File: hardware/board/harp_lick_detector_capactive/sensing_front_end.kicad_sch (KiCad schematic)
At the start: 33 parts

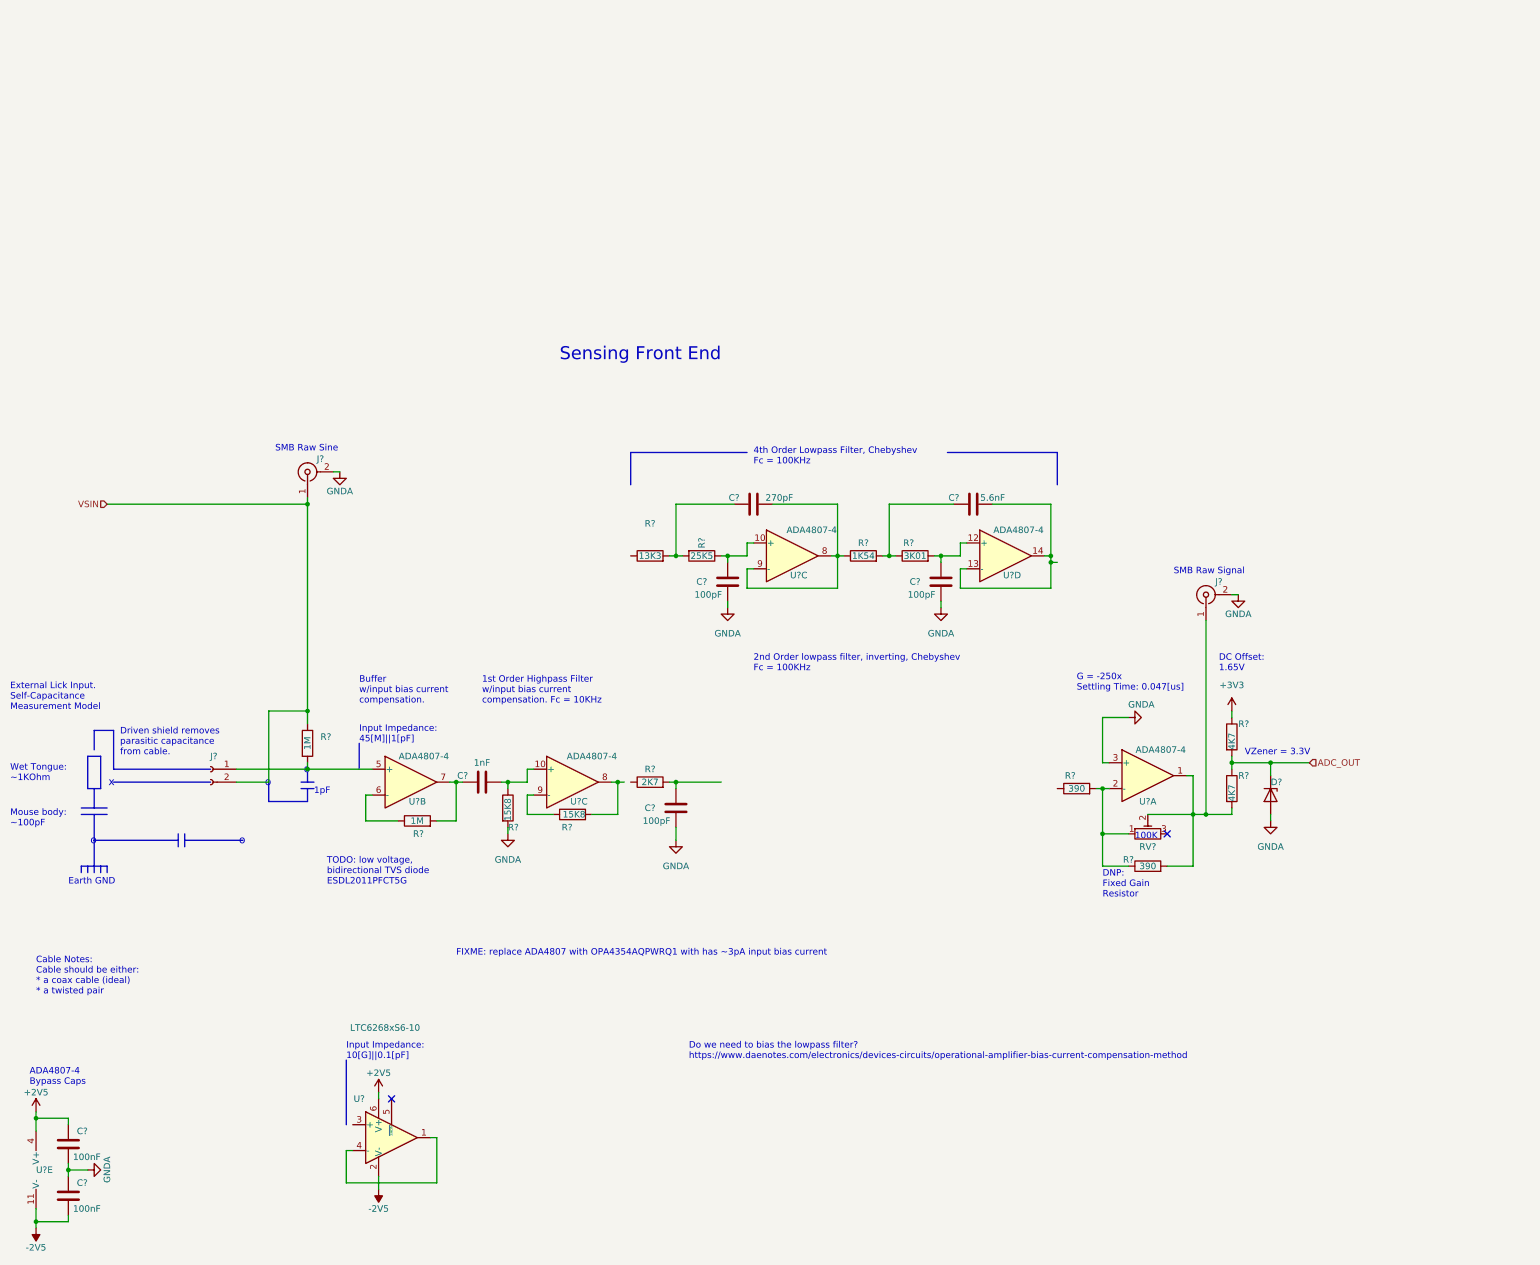
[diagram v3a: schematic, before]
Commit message: document stray capacitances
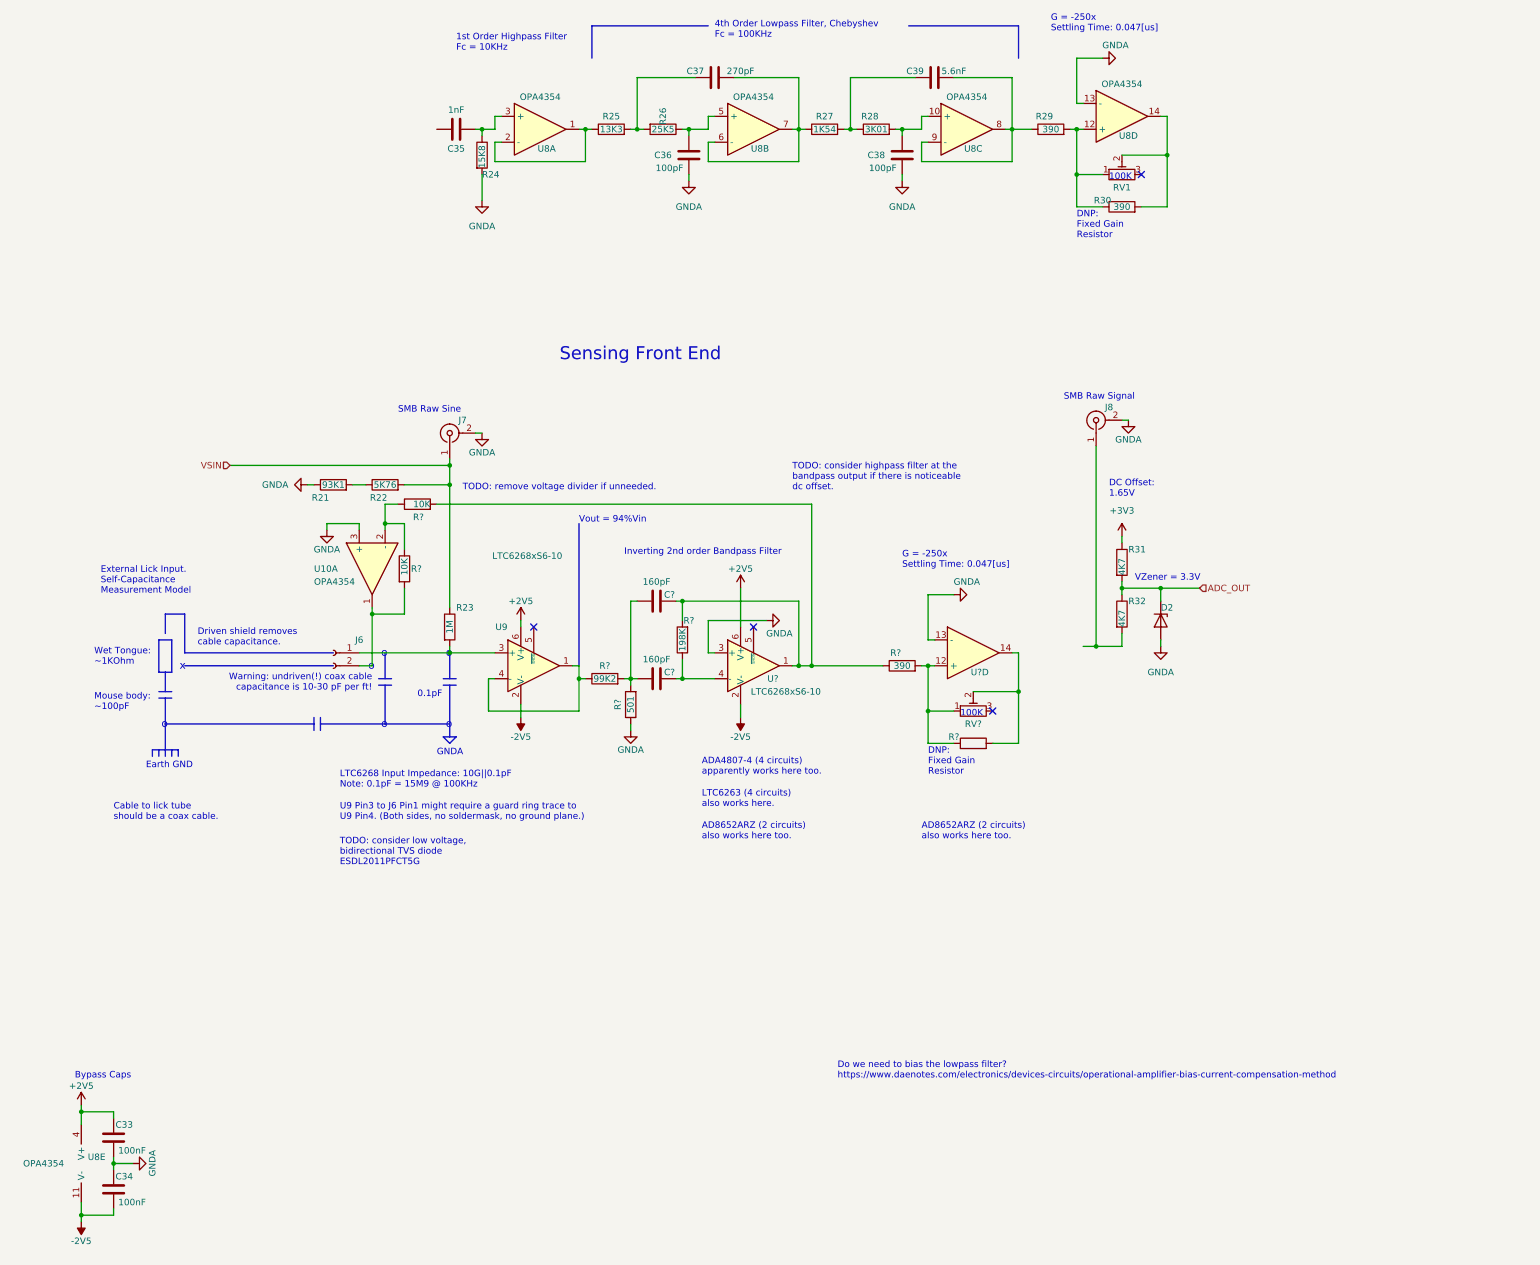
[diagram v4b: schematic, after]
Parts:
- removed C?: 100pF, Capacitor_SMD:C_0603_1608Metric_Pad1.08x0.95mm_HandSolder, symbol Device:C
- removed R?: 2K7, symbol Device:R
- removed R?: 15K8, symbol Device:R
- removed R?: 1M, Resistor_SMD:R_0603_1608Metric_Pad0.98x0.95mm_HandSolder, symbol Device:R
- removed U? (x6): ADA4807-4, Package_SO:TSSOP-14_4.4x5mm_P0.65mm, symbol Amplifier_Operational:ADA4807-4
- added C? (x2): 160pF, Capacitor_SMD:C_0402_1005Metric_Pad0.74x0.62mm_HandSolder, symbol Device:C
- added R21: 93K1, symbol Device:R
- added R22: 5K76, symbol Device:R
- added R?: ~, symbol Device:R
- added R?: 99K2, symbol Device:R
- added R?: 198K, symbol Device:R
- added R?: 501, symbol Device:R
- added R?: 390, symbol Device:R
- added R? (x2): 10K, Resistor_SMD:R_0402_1005Metric_Pad0.72x0.64mm_HandSolder, symbol Device:R
- added RV?: ~, symbol Device:R_Potentiometer_Trim
- added U10, U8: OPA4354, symbol machine_agency_components:OPA4354
- added U?: ~, symbol machine_agency_components:OPA4354
- added U?: LTC6268xS6-10, symbol Amplifier_Operational:LTC6268xS6-10
- gave numbers to parts that had none: 23
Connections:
- net +2V5: now also U8.4 (V+), U?.6 (V+)
- net -2V5: now also U8.11 (V-), U?.2 (V-)
- net GNDA: now also R21.1, R?.1, U10.3 (+), U8.13 (-), U?.13 (-), U?.3 (+)
- net VSIN: now also R22.2; no longer J6.2 (Pin_2)
- net at C38.2, R28.2: now also U8.10 (+)
- net at C39.2: now also R29.1, U8.8, U8.9 (-)
- net at U9.1, U9.4 (-): now also R?.1
- net at U9.3 (+): now also J6.1 (Pin_1), R23.2
- net at R25.1: now also U8.1, U8.2 (-)
- net at C36.2, R26.1: now also U8.5 (+)
- net at C35.2, R24.1: now also U8.3 (+)
- net at R30.2, RV1.2: now also U8.14; no longer J8.1 (In), R32.2
- net at R29.2, R30.1, RV1.1: now also U8.12 (+)
- net at C37.2, R27.1: now also U8.6 (-), U8.7
- new net: R?.1, R?.2, RV?.1, U?.12 (+)
- new net: R?.2, RV?.2, U?.14
- new net: J6.2 (Pin_2), R?.2, U10.1
- new net: R?.1, R?.1, U10.2 (-)
- new net: C?.1, C?.1, R?.2, R?.2
- new net: C?.2, R?.1, U?.4 (-)
- new net: C?.2, R?.1, R?.2, R?.2, U?.1
- new net: R21.2, R22.1
- new net: J8.1 (In), R32.2
- no-connect marks 2 -> 4
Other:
- note added: "0.1pF"
- note added: "1st Order Highpass Filter Fc = 10KHz"
- note added: "AD8652ARZ (2 circuits) also works here too."
- note added: "ADA4807-4 (4 circuits) apparently works here too."
- note added: "Bypass Caps"
- note added: "Cable to lick tube should be a coax cable."
- note added: "Driven shield removes cable capacitance."
- note added: "GNDA"
- note added: "Inverting 2nd order Bandpass Filter"
- note added: "LTC6263 (4 circuits) also works here."
- note added: "LTC6268 Input Impedance: 10G||0.1pF Note: 0.1pF = 15M9 @ 100KHz"
- note added: "TODO: consider highpass filter at the bandpass output if there is noticeable dc offset."
- note added: "TODO: consider low voltage, bidirectional TVS diode ESDL2011PFCT5G"
- note added: "TODO: remove voltage divider if unneeded."
- note added: "U9 Pin3 to J6 Pin1 might require a guard ring trace to U9 Pin4. (Both sides, no soldermask, no ground plane.)"
- note added: "Vout = 94%Vin"
- note added: "Warning: undriven(!) coax cable capacitance is 10-30 pF per ft!"
- note removed: "1pF"
- note removed: "1st Order Highpass Filter w/input bias current compensation. Fc = 10KHz"
- note removed: "2nd Order lowpass filter, inverting, Chebyshev Fc = 100KHz"
- note removed: "ADA4807-4 Bypass Caps"
- note removed: "Buffer w/input bias current compensation."
- note removed: "Cable Notes: Cable should be either: * a coax cable (ideal) * a twisted pair"
- note removed: "Driven shield removes parasitic capacitance from cable."
- note removed: "FIXME: replace ADA4807 with OPA4354AQPWRQ1 with has ~3pA input bias current"
- note removed: "Input Impedance: 10[G]||0.1[pF]"
- note removed: "Input Impedance: 45[M]||1[pF]"
- note removed: "TODO: low voltage, bidirectional TVS diode ESDL2011PFCT5G"
- moved on the sheet: C33, C34, C35, C36, C37, C38, C39, D2, J6, J7, J8, R23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

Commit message: pass eeschema drc
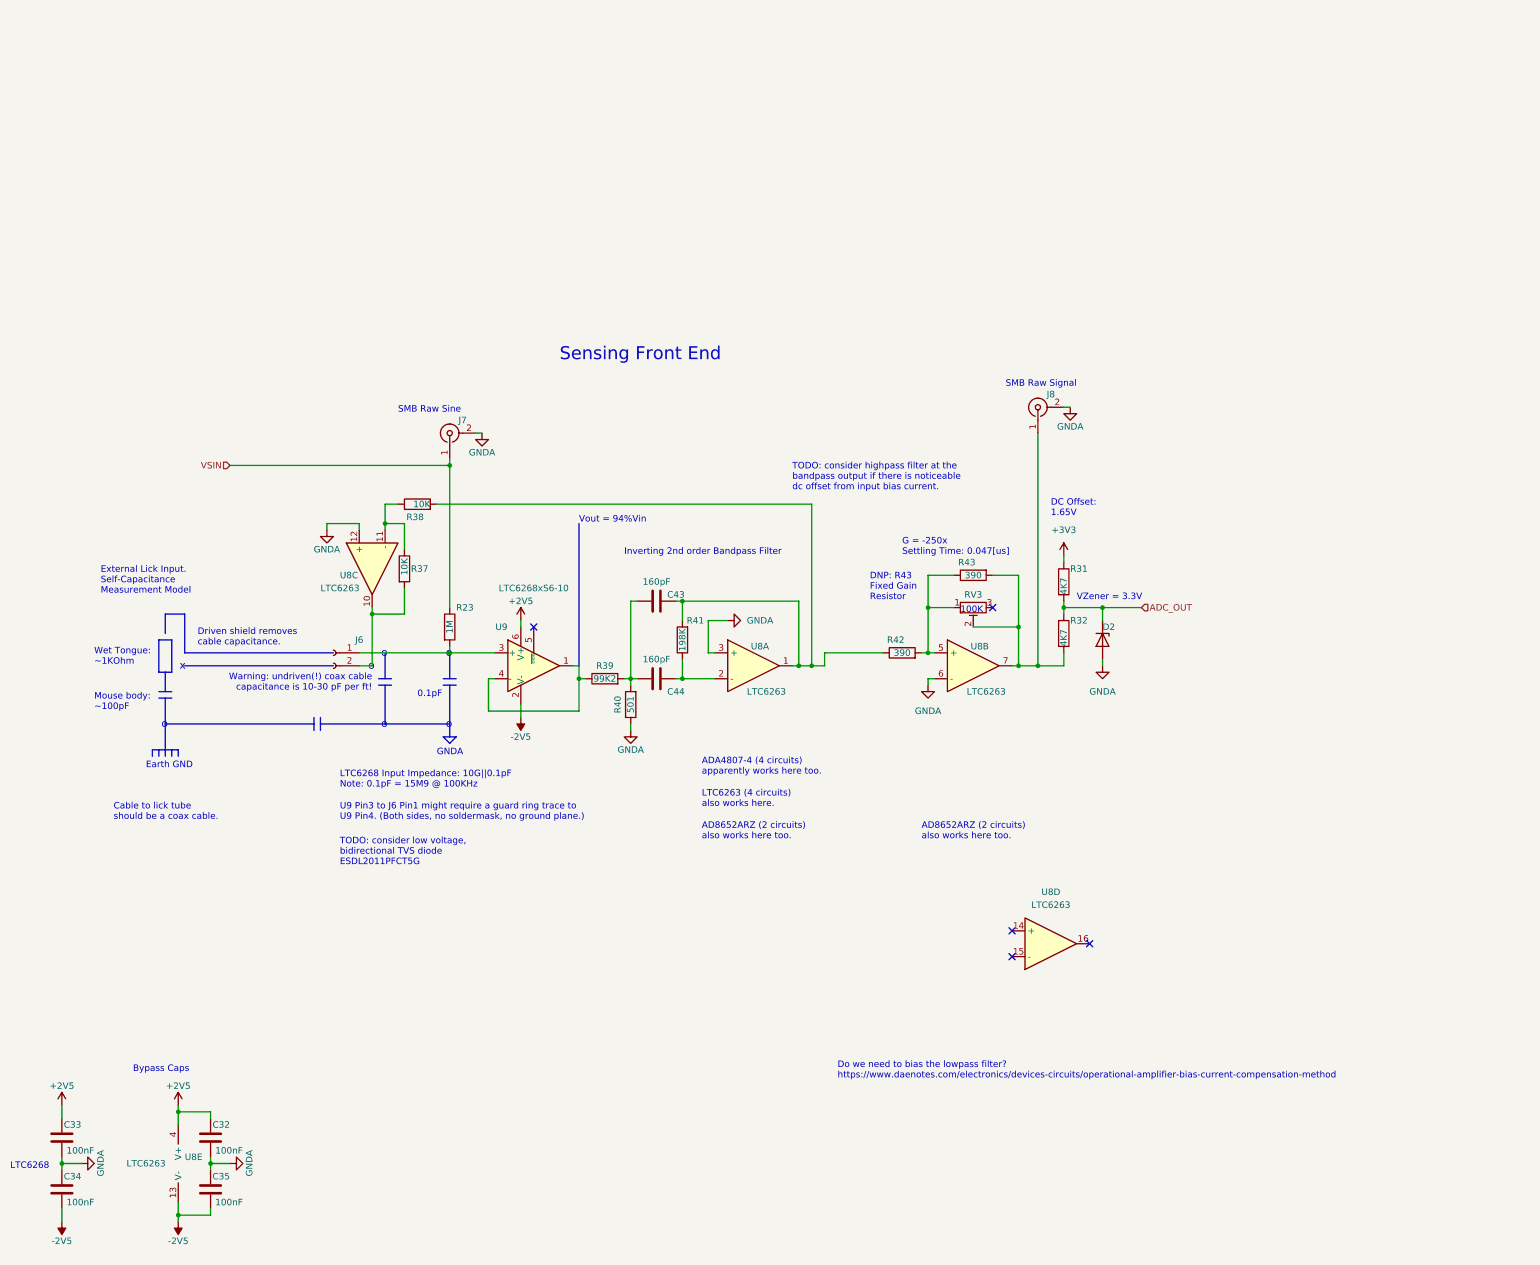
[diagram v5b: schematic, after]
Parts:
- removed C36, C38: 100pF, Capacitor_SMD:C_0603_1608Metric_Pad1.08x0.95mm_HandSolder, symbol Device:C
- removed C37: 270pF, symbol Device:C
- removed C39: 5.6nF, symbol Device:C
- removed R21: 93K1, symbol Device:R
- removed R22: 5K76, symbol Device:R
- removed R24: 15K8, symbol Device:R
- removed R25: 13K3, symbol Device:R
- removed R26: 25K5, symbol Device:R
- removed R27: 1K54, symbol Device:R
- removed R28: 3K01, symbol Device:R
- removed R29, R30: 390, Resistor_SMD:R_0603_1608Metric_Pad0.98x0.95mm_HandSolder, symbol Device:R
- removed RV1: R_Potentiometer_Trim, Potentiometer_SMD:Potentiometer_Bourns_3314G_Vertical, symbol Device:R_Potentiometer_Trim
- removed U10, U8: OPA4354, symbol machine_agency_components:OPA4354
- removed U?: ~, symbol machine_agency_components:OPA4354
- removed U?: LTC6268xS6-10, symbol Amplifier_Operational:LTC6268xS6-10
- added C32: 100nF, Capacitor_SMD:C_0603_1608Metric_Pad1.08x0.95mm_HandSolder, symbol Device:C
- added U8: LTC6263, Package_SO:MSOP-16_3x4mm_P0.5mm, symbol machine_agency_components:LTC6263
- C35: value 1nF -> 100nF; footprint (none) -> Capacitor_SMD:C_0603_1608Metric_Pad1.08x0.95mm_HandSolder; Link (none) -> https://www.digikey.com/en/products/detail/samsung-electro-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; Manufacturer (none) -> Samsung Electro-Mechanics; Manufacturer Number (none) -> CL10B104KB8NNWC; Rated Voltage (none) -> 50V; Temperature Coefficient (none) -> X7R; Tolerance (none) -> 10%
- R42: renamed from R?; footprint (none) -> Resistor_SMD:R_0603_1608Metric_Pad0.98x0.95mm_HandSolder
- R43: renamed from R?; value ~ -> 390; footprint (none) -> Resistor_SMD:R_0603_1608Metric_Pad0.98x0.95mm_HandSolder
- RV3: renamed from RV?; footprint (none) -> Potentiometer_SMD:Potentiometer_Bourns_3314G_Vertical
- gave numbers to parts that had none: 7
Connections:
- net +2V5: now also C32.2, U8.4 (V+)
- net -2V5: now also C35.1, U8.13 (V-)
- net GNDA: now also C35.2, C32.1, U8.12 (+), U8.3 (+), U8.6 (-)
- net at R42.2, R43.1, RV3.1: now also U8.5 (+)
- net at R43.2, RV3.2: now also J8.1 (In), R32.2, U8.7
- net at J6.2 (Pin_2), R37.2: now also U8.10
- net at R37.1, R38.1: now also U8.11 (-)
- net at C44.2, R41.1: now also U8.2 (-)
- net at C43.2, R38.2, R41.2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: now also U8.1
- no-connect marks 4 -> 5
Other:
- note added: "DNP: R43 Fixed Gain Resistor"
- note added: "LTC6268"
- note added: "TODO: consider highpass filter at the bandpass output if there is noticeable dc offset from input bias current."
- note removed: "1st Order Highpass Filter Fc = 10KHz"
- note removed: "4th Order Lowpass Filter, Chebyshev Fc = 100KHz"
- note removed: "DNP: Fixed Gain Resistor"
- note removed: "TODO: consider highpass filter at the bandpass output if there is noticeable dc offset."
- note removed: "TODO: remove voltage divider if unneeded."
- moved on the sheet: C33, C34, D2, J8, R31, R32, R42, R43, RV3

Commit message: complete bom assignment
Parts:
- removed J6: Conn_01x02_Female, symbol Connector:Conn_01x02_Female
- added J6: (no value), symbol Connector:Conn_Coaxial
- C32, C33, C34, C35: value 100nF -> (none); footprint Capacitor_SMD:C_0603_1608Metric_Pad1.08x0.95mm_HandSolder -> (none)
- C43, C44: value 160pF -> (none); footprint Capacitor_SMD:C_0402_1005Metric_Pad0.74x0.62mm_HandSolder -> (none)
- D2: value BZX384-A3V3-QX -> (none); footprint Diode_SMD:D_SOD-323_HandSoldering -> (none)
- J7, J8: value Conn_Coaxial -> (none); footprint Connector_Coaxial:SMA_Amphenol_901-143_Horizontal -> (none)
- R23: value 1M -> (none); footprint Resistor_SMD:R_0603_1608Metric_Pad0.98x0.95mm_HandSolder -> (none); Tolerance (none) -> 1%
- R31, R32: value 4K7 -> (none); footprint Resistor_SMD:R_0603_1608Metric_Pad0.98x0.95mm_HandSolder -> (none)
- R37, R38: value 10K -> (none); footprint Resistor_SMD:R_0402_1005Metric_Pad0.72x0.64mm_HandSolder -> (none)
- R39: value 99K2 -> (none); Link (none) -> https://www.digikey.com/en/products/detail/koa-speer-electr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; Manufacturer (none) -> KOA Spear Electronics, Inc.; Manufacturer Number (none) -> RN73H1JTTD9882B25; Notes (none) -> ideally would be 99K2; Tolerance (none) -> 0.1%
- R40: value 501 -> (none); Link (none) -> https://www.digikey.com/en/products/detail/yageo/RT0603BRC0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; Manufacturer (none) -> Yageo; Manufacturer Number (none) -> RT0603BRC07500RL; Notes (none) -> Ideally would be 501; Tolerance (none) -> 0.1%
- R41: value 198K -> (none); Link (none) -> https://www.digikey.com/en/products/detail/yageo/RT0603BRD0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; Manufacturer (none) -> Yageo; Manufacturer Number (none) -> RT0603BRD07200KL; Notes (none) -> ideally would be 198K; Tolerance (none) -> 0.1%
- R42, R43: value 390 -> (none); footprint Resistor_SMD:R_0603_1608Metric_Pad0.98x0.95mm_HandSolder -> (none)
- RV3: value ~ -> (none); footprint Potentiometer_SMD:Potentiometer_Bourns_3314G_Vertical -> (none)
- U8: value LTC6263 -> (none); footprint Package_SO:MSOP-16_3x4mm_P0.5mm -> (none)
- U9: value LTC6268xS6-10 -> (none); Link (none) -> https://www.digikey.com/en/products/detail/analog-devices-i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
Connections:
- net at R23.2, U9.3 (+): now also J6.1 (In)
- net at R37.2, U8.10: now also J6.2 (Ext)
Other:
- note added: "R39 ideal: 99K2 R40 ideal: 501 R41 ideal: 198K"
- moved on the sheet: C43, C44, D2, J7, J8, R23, R31, R32, R37, R38, R39, R40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
